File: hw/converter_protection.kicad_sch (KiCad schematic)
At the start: 103 parts, among them Q901 BSS127S, Q902 BSS127S, Q903 Q_NMOS_GDS, Q904 Q_NMOS_GDS, Q905 Q_NMOS_GDS, Q906 Q_NMOS_GDS, Q907 BSS127S, Q908 BSS127S, Q909 BSS127S, Q910 BSS127S, U901 TLV9022, U902 TLV9022, U903 TLV9022, U904 TPSI3050, U905 TPSI3050, U906 TPSI3050, U907 TPSI3050

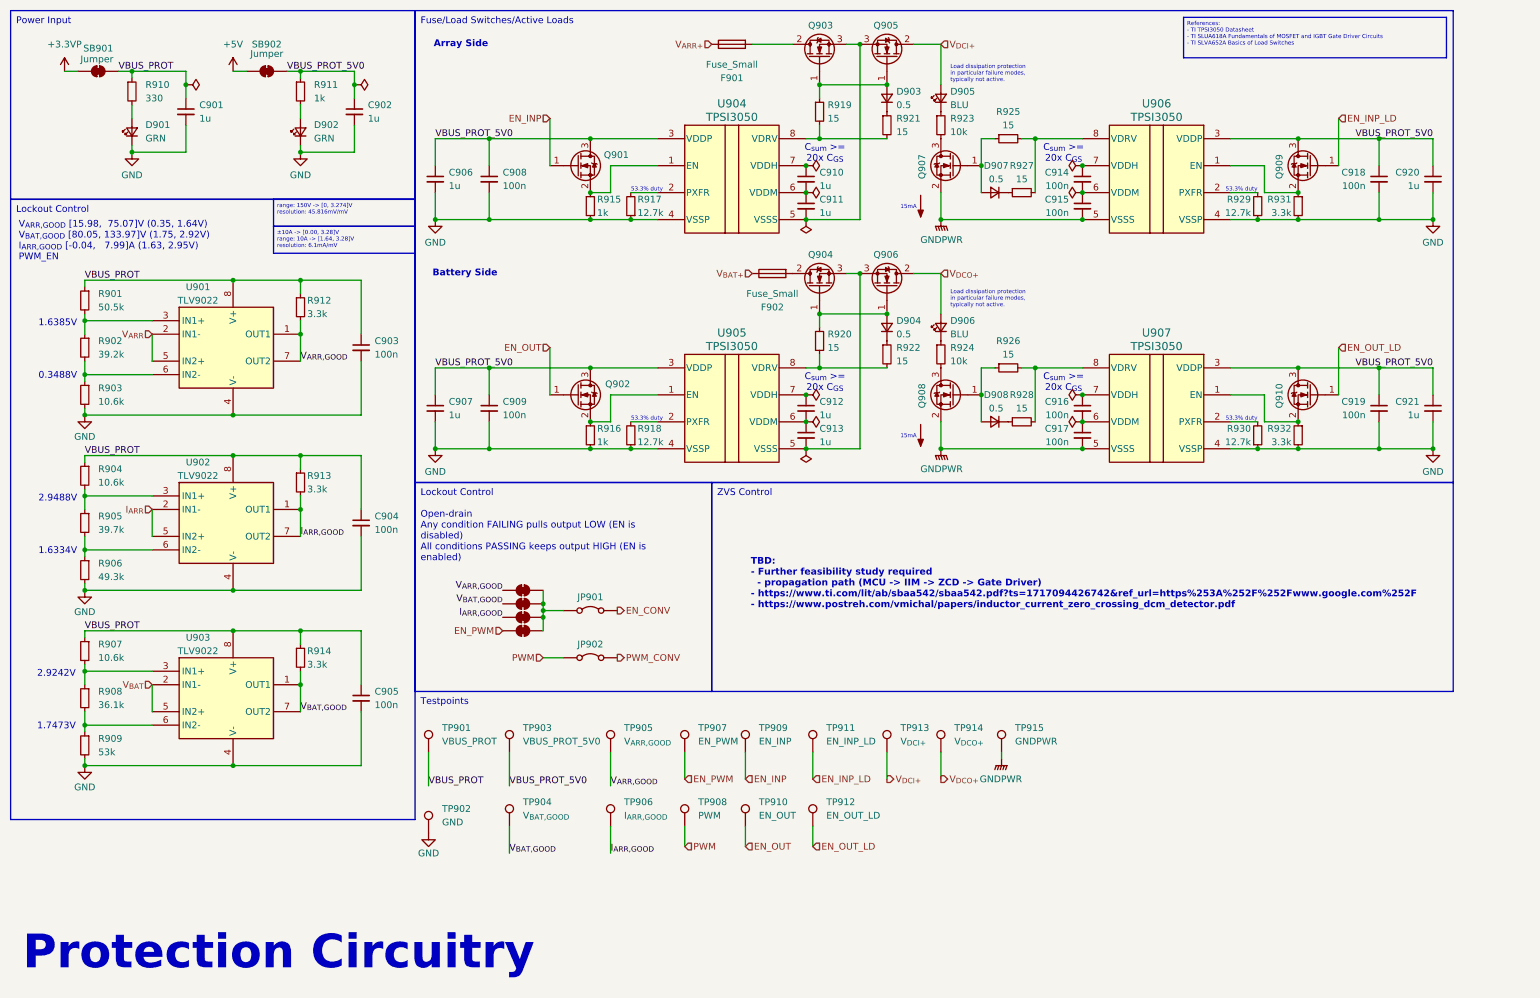
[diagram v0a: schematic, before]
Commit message: HW sch changes, further layout progression
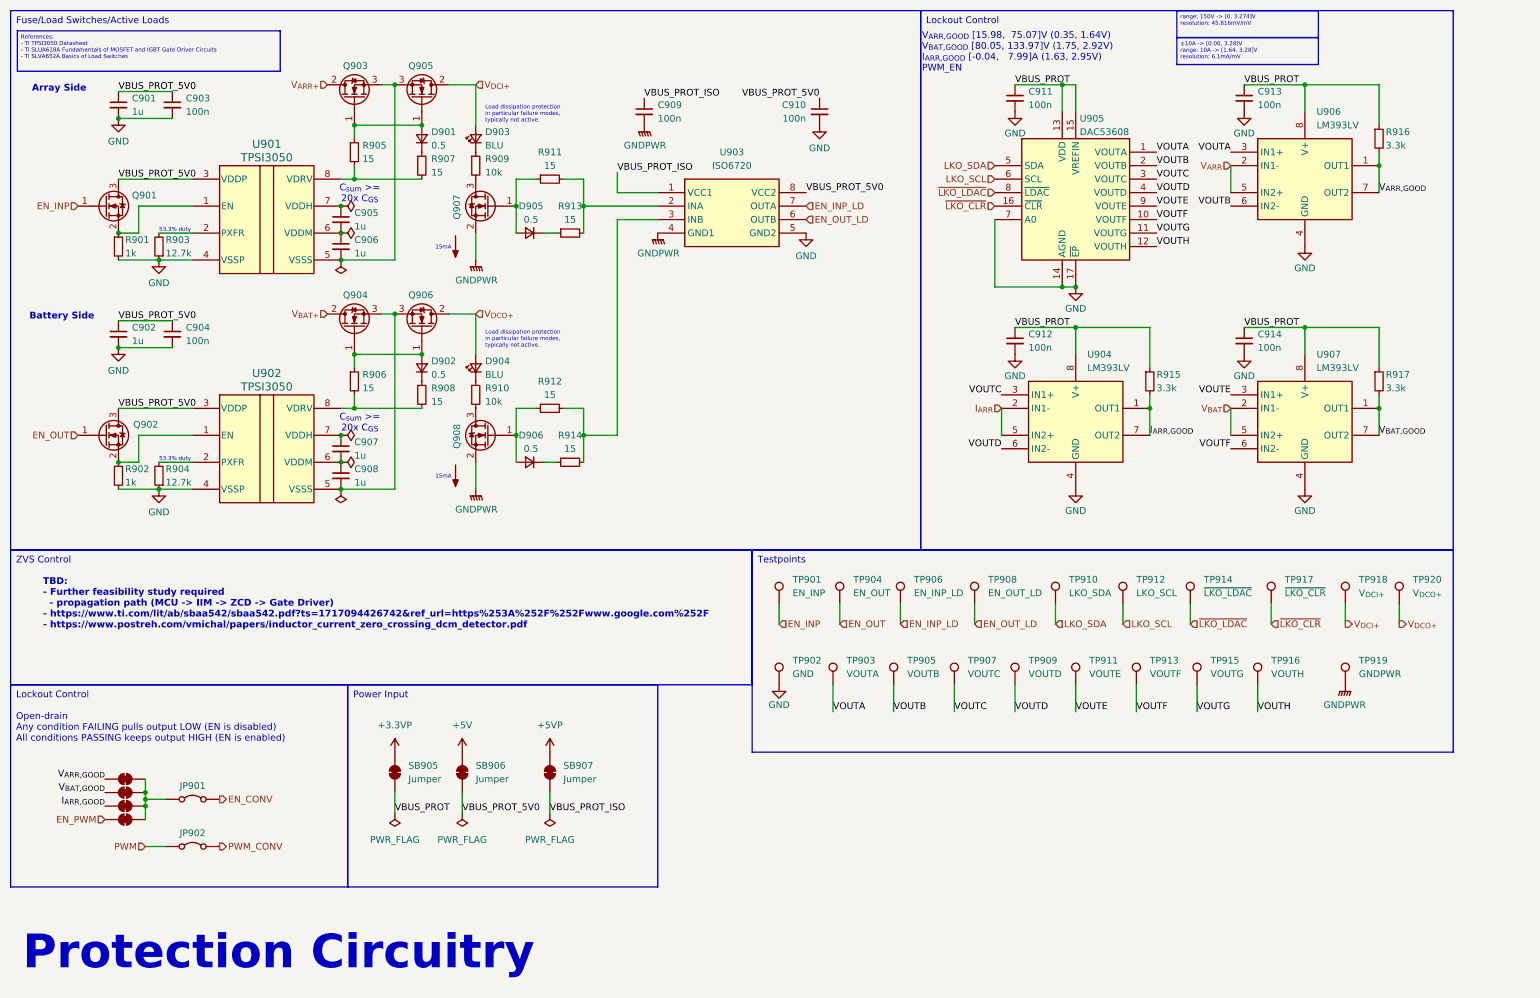
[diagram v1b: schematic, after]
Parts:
- removed C905, C908, C915, C916, C917, C918, C919: 100n, Resistor_SMD:R_0402_1005Metric, symbol Device:C_Small
- removed C906, C907, C920, C921: 1u, Resistor_SMD:R_0402_1005Metric, symbol Device:C_Small
- removed D901, D902: GRN, LED_SMD:LED_0402_1005Metric, symbol Device:LED_Small
- removed F901, F902: Fuse_Small, footprints:littelfuse_05200101Z, symbol Device:Fuse
- removed Q909, Q910: BSS127S, Package_TO_SOT_SMD:SOT-23, symbol Device:Q_NMOS_GSD
- removed R901: 50.5k, Resistor_SMD:R_0402_1005Metric, symbol Device:R_Small
- removed R902: 39.2k, Resistor_SMD:R_0402_1005Metric, symbol Device:R_Small
- removed R903, R904, R907: 10.6k, Resistor_SMD:R_0603_1608Metric, symbol Device:R_Small
- removed R905: 39.7k, Resistor_SMD:R_0402_1005Metric, symbol Device:R_Small
- removed R906: 49.3k, Resistor_SMD:R_0603_1608Metric, symbol Device:R_Small
- removed R908: 36.1k, Resistor_SMD:R_0805_2012Metric, symbol Device:R_Small
- removed R909: 53k, Resistor_SMD:R_0603_1608Metric, symbol Device:R_Small
- removed R910: 330, Resistor_SMD:R_0402_1005Metric, symbol Device:R_Small
- removed R911: 1k, Resistor_SMD:R_0402_1005Metric, symbol Device:R_Small
- removed R912, R913, R914, R931, R932: 3.3k, Resistor_SMD:R_0402_1005Metric, symbol Device:R_Small
- removed R929, R930: 12.7k, Resistor_SMD:R_0402_1005Metric, symbol Device:R_Small
- removed SB901, SB902: Jumper, Jumper:SolderJumper-2_P1.3mm_Open_TrianglePad1.0x1.5mm, symbol Jumper:SolderJumper_2_Bridged
- removed TP901: VBUS_PROT, TestPoint:TestPoint_Keystone_5000-5004_Miniature, symbol Connector:TestPoint
- removed TP904: V_{BAT,GOOD}, TestPoint:TestPoint_Keystone_5000-5004_Miniature, symbol Connector:TestPoint
- removed TP906: I_{ARR,GOOD}, TestPoint:TestPoint_Keystone_5000-5004_Miniature, symbol Connector:TestPoint
- removed TP908: PWM, TestPoint:TestPoint_Keystone_5000-5004_Miniature, symbol Connector:TestPoint
- removed U901, U902, U903: TLV9022, footprints:ti_TLV9022_DR, symbol ti_TLV9022:TLV9022DR
- removed U906, U907: TPSI3050, footprints:ti_TPS3050_DWZ, symbol ti_TPS3050:TPSI3050QDWZRQ1
- added C910, C911, C912, C913: 100n, Resistor_SMD:R_0402_1005Metric, symbol Device:C_Small
- added R915, R916, R917: 3.3k, Resistor_SMD:R_0402_1005Metric, symbol Device:R_Small
- added SB905, SB906, SB907: Jumper, Jumper:SolderJumper-2_P1.3mm_Open_TrianglePad1.0x1.5mm, symbol Jumper:SolderJumper_2_Bridged
- added TP909: VOUTD, TestPoint:TestPoint_Pad_D1.5mm, symbol Connector:TestPoint
- added TP910: LKO_SDA, TestPoint:TestPoint_Pad_D1.5mm, symbol Connector:TestPoint
- added TP911: VOUTE, TestPoint:TestPoint_Pad_D1.5mm, symbol Connector:TestPoint
- added TP912: LKO_SCL, TestPoint:TestPoint_Pad_D1.5mm, symbol Connector:TestPoint
- added TP913: VOUTF, TestPoint:TestPoint_Pad_D1.5mm, symbol Connector:TestPoint
- added TP914: ~{LKO_LDAC}, TestPoint:TestPoint_Pad_D1.5mm, symbol Connector:TestPoint
- added TP915: VOUTG, TestPoint:TestPoint_Pad_D1.5mm, symbol Connector:TestPoint
- added TP916: VOUTH, TestPoint:TestPoint_Pad_D1.5mm, symbol Connector:TestPoint
- added TP917: ~{LKO_CLR}, TestPoint:TestPoint_Pad_D1.5mm, symbol Connector:TestPoint
- added U903: ISO6720, footprints:ti_ISO6720B_DR, symbol ti_ISO6720:ISO6720FBDR
- added U904, U906, U907: LM393LV, footprints:ti_LM393LV_DR, symbol ti_LM393LV:LM393LVQDRQ1
- added U905: DAC53608, footprints:ti_DAC53608_RT, symbol ti_DAC53608:DAC53608RTER
- C901, C902: Notes Bulk capacitance. -> (none)
- C903, C904: Notes Recommended value. -> (none)
- C914: Notes Sized according to TPSI305x calculator spreadsheet (16.4nC,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 -> Recommended value.
- R903: renamed from R917; footprint Resistor_SMD:R_0402_1005Metric -> Resistor_SMD:R_0402_1005Metric
- R904: renamed from R918; footprint Resistor_SMD:R_0402_1005Metric -> Resistor_SMD:R_0402_1005Metric
- TP901: renamed from TP909; footprint TestPoint:TestPoint_Keystone_5000-5004_Miniature -> TestPoint:TestPoint_Pad_D1.5mm; Cost 0.38 -> (none); Distributor Mouser -> (none); Manufacturer Keystone Electronics -> (none); Notes White (Digital Signal) -> (none); P/N 5002 -> (none)
- TP902: footprint TestPoint:TestPoint_Keystone_5000-5004_Miniature -> TestPoint:TestPoint_Pad_D1.5mm; Cost 0.37 -> (none); Distributor Mouser -> (none); Manufacturer Keystone Electronics -> (none); Notes Black (Logic Ground) -> (none); P/N 5001 -> (none)
- TP903: value VBUS_PROT_5V0 -> VOUTA; footprint TestPoint:TestPoint_Keystone_5000-5004_Miniature -> TestPoint:TestPoint_Pad_D1.5mm; Cost 0.31 -> (none); Distributor Mouser -> (none); Manufacturer Keystone Electronics -> (none); Notes Red (Logic Power) -> (none); P/N 5000 -> (none)
- TP904: renamed from TP910; footprint TestPoint:TestPoint_Keystone_5000-5004_Miniature -> TestPoint:TestPoint_Pad_D1.5mm; Cost 0.38 -> (none); Distributor Mouser -> (none); Manufacturer Keystone Electronics -> (none); Notes White (Digital Signal) -> (none); P/N 5002 -> (none)
- TP905: value V_{ARR,GOOD} -> VOUTB; footprint TestPoint:TestPoint_Keystone_5000-5004_Miniature -> TestPoint:TestPoint_Pad_D1.5mm; Cost 0.38 -> (none); Distributor Mouser -> (none); Manufacturer Keystone Electronics -> (none); Notes White (Digital Signal) -> (none); P/N 5002 -> (none)
- TP906: renamed from TP911; footprint TestPoint:TestPoint_Keystone_5000-5004_Miniature -> TestPoint:TestPoint_Pad_D1.5mm; Cost 0.38 -> (none); Distributor Mouser -> (none); Manufacturer Keystone Electronics -> (none); Notes White (Digital Signal) -> (none); P/N 5002 -> (none)
- TP907: value EN_PWM -> VOUTC; footprint TestPoint:TestPoint_Keystone_5000-5004_Miniature -> TestPoint:TestPoint_Pad_D1.5mm; Cost 0.38 -> (none); Distributor Mouser -> (none); Manufacturer Keystone Electronics -> (none); Notes White (Digital Signal) -> (none); P/N 5002 -> (none)
- TP908: renamed from TP912; footprint TestPoint:TestPoint_Keystone_5000-5004_Miniature -> TestPoint:TestPoint_Pad_D1.5mm; Cost 0.38 -> (none); Distributor Mouser -> (none); Manufacturer Keystone Electronics -> (none); Notes White (Digital Signal) -> (none); P/N 5002 -> (none)
- TP918: renamed from TP913; footprint TestPoint:TestPoint_Keystone_5000-5004_Miniature -> TestPoint:TestPoint_Pad_D1.5mm; Cost 0.36 -> (none); Distributor Mouser -> (none); Manufacturer Keystone Electronics -> (none); Notes Blue (Power Path Measurement) -> (none); P/N 5117 -> (none)
- TP919: renamed from TP915; footprint TestPoint:TestPoint_Keystone_5000-5004_Miniature -> TestPoint:TestPoint_Pad_D1.5mm; Cost 0.37 -> (none); Distributor Mouser -> (none); Manufacturer Keystone Electronics -> (none); Notes Brown (Power Path Ground) -> (none); P/N 5115 -> (none)
- TP920: renamed from TP914; footprint TestPoint:TestPoint_Keystone_5000-5004_Miniature -> TestPoint:TestPoint_Pad_D1.5mm; Cost 0.36 -> (none); Distributor Mouser -> (none); Manufacturer Keystone Electronics -> (none); Notes Blue (Power Path Measurement) -> (none); P/N 5117 -> (none)
- renumbered C910 to C905, C911 to C906, C912 to C907, C913 to C908, D903 to D901, D904 to D902, D905 to D903, D906 to D904, D907 to D905, D908 to D906, R915 to R901, R916 to R902, R919 to R905, R920 to R906, R921 to R907, R922 to R908, R923 to R909, R924 to R910, R925 to R911, R926 to R912, R927 to R913, R928 to R914, SB903 to SB901, SB904 to SB902, SB905 to SB903, SB906 to SB904, U904 to U901, U905 to U902
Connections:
- net +3.3VP: now also SB905.2 (B)
- net +5V: now also SB906.2 (B)
- net EN_INP_LD: now also U903.7 (OUTA)
- net EN_OUT_LD: now also U903.6 (OUTB)
- net EN_PWM: no longer TP907.1
- net GND: now also C914.2, C910.2, C911.2, C912.2, C913.2, U903.5 (GND2), U904.4 (GND), U905.14 (AGND), U905.17 (~{EP}), U905.7 (A0), U906.4 (GND), U907.4 (GND); no longer C909.2
- net GNDPWR: now also C909.2, U903.4 (GND1)
- net I_{ARR,GOOD}: now also R915.2, U904.1 (OUT1), U904.7 (OUT2)
- net I_{ARR}: now also U904.2 (IN1-), U904.5 (IN2+)
- net VBUS_PROT: now also C914.1, C911.1, C912.1, C913.1, R915.1, R916.1, R917.1, SB905.1 (A), U904.8 (V+), U905.13 (VDD), U905.15 (VREFIN), U906.8 (V+), U907.8 (V+); no longer C901.1, C903.1, C904.1
- net VBUS_PROT_5V0: now also C901.1, C903.1, C904.1, C910.1, SB906.1 (A), U903.8 (VCC2); no longer C909.1, TP903.1
- net V_{ARR+}: now also Q903.2 (D)
- net V_{ARR,GOOD}: now also R916.2, U906.1 (OUT1), U906.7 (OUT2); no longer TP905.1
- net V_{ARR}: now also U906.2 (IN1-), U906.5 (IN2+)
- net V_{BAT+}: now also Q904.2 (D)
- net V_{BAT,GOOD}: now also R917.2, U907.1 (OUT1), U907.7 (OUT2)
- net V_{BAT}: now also U907.2 (IN1-), U907.5 (IN2+)
- net at R911.2, R913.2: now also U903.2 (INA)
- net at R912.2, R914.2: now also U903.3 (INB)
- new net +5VP: SB907.2 (B)
- new net LKO_SCL: TP912.1, U905.6 (SCL)
- new net LKO_SDA: TP910.1, U905.5 (SDA)
- new net VBUS_PROT_ISO: C909.1, SB907.1 (A), U903.1 (VCC1)
- new net VOUTA: TP903.1, U905.1 (VOUTA), U906.3 (IN1+)
- new net VOUTB: TP905.1, U905.2 (VOUTB), U906.6 (IN2-)
- new net VOUTC: TP907.1, U904.3 (IN1+), U905.3 (VOUTC)
- new net VOUTD: TP909.1, U904.6 (IN2-), U905.4 (VOUTD)
- new net VOUTE: TP911.1, U905.9 (VOUTE), U907.3 (IN1+)
- new net VOUTF: TP913.1, U905.10 (VOUTF), U907.6 (IN2-)
- new net VOUTG: TP915.1, U905.11 (VOUTG)
- new net VOUTH: TP916.1, U905.12 (VOUTH)
- new net ~{LKO_CLR}: TP917.1, U905.16 (~{CLR})
- new net ~{LKO_LDAC}: TP914.1, U905.8 (~{LDAC})
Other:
- note removed: "0.3488V"
- note removed: "1.6334V"
- note removed: "1.6385V"
- note removed: "1.7473V"
- note removed: "2.9242V"
- note removed: "2.9488V"
- moved on the sheet: C905, C906, C907, C908, D901, D902, D903, D904, D905, D906, JP901, JP902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
